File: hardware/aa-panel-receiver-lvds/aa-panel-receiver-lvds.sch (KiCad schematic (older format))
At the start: 100 parts, among them CN101 Conn_01x02, CN102 Conn_01x02, CN201 8P8C, CN202 Conn_01x08, CN251 Conn_01x08, CN301 8P8C, CN302 Conn_01x08, CN351 Conn_01x08, U101 CRE1S0505S3C, U201 ST26C32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

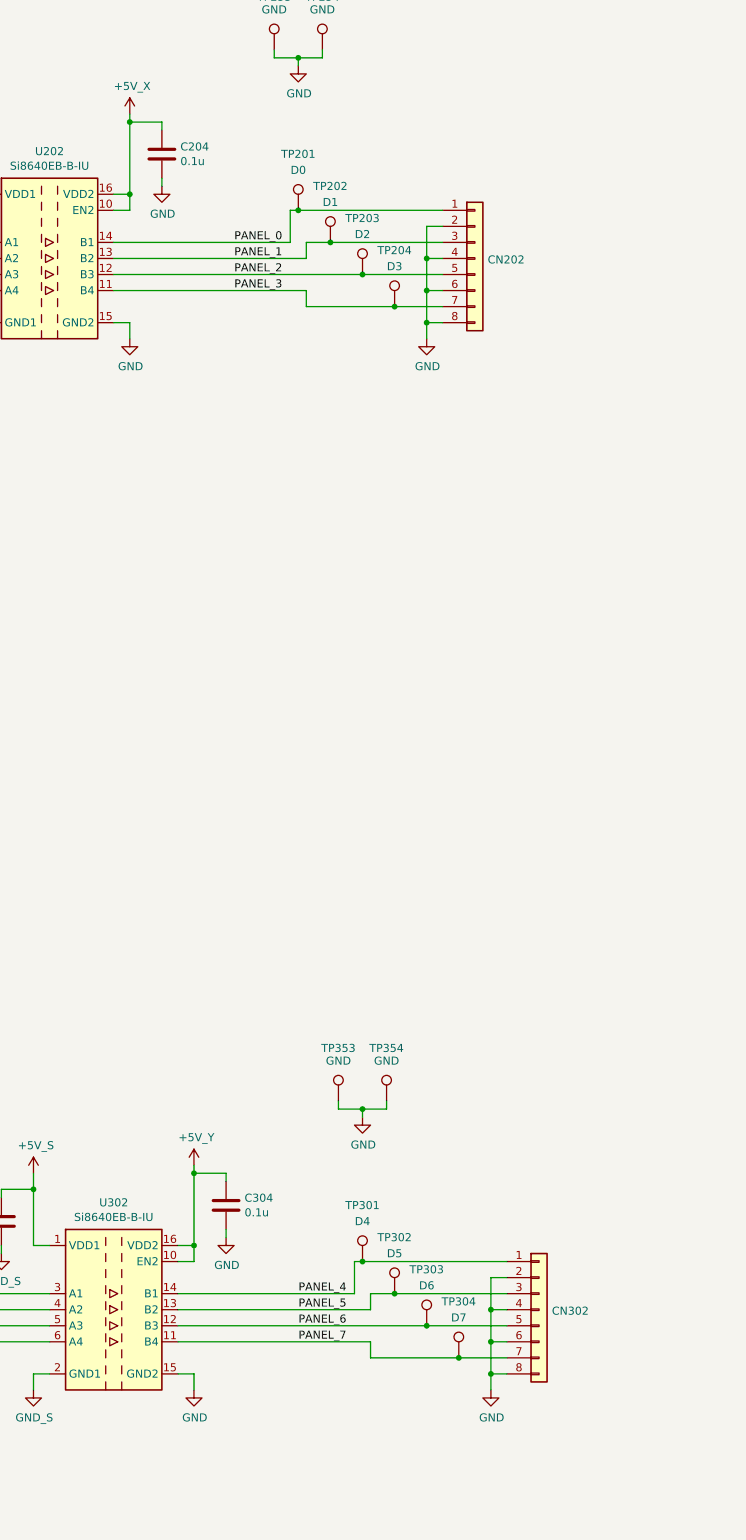
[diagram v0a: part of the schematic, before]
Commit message: Minor board updates to fix issues discovered during build
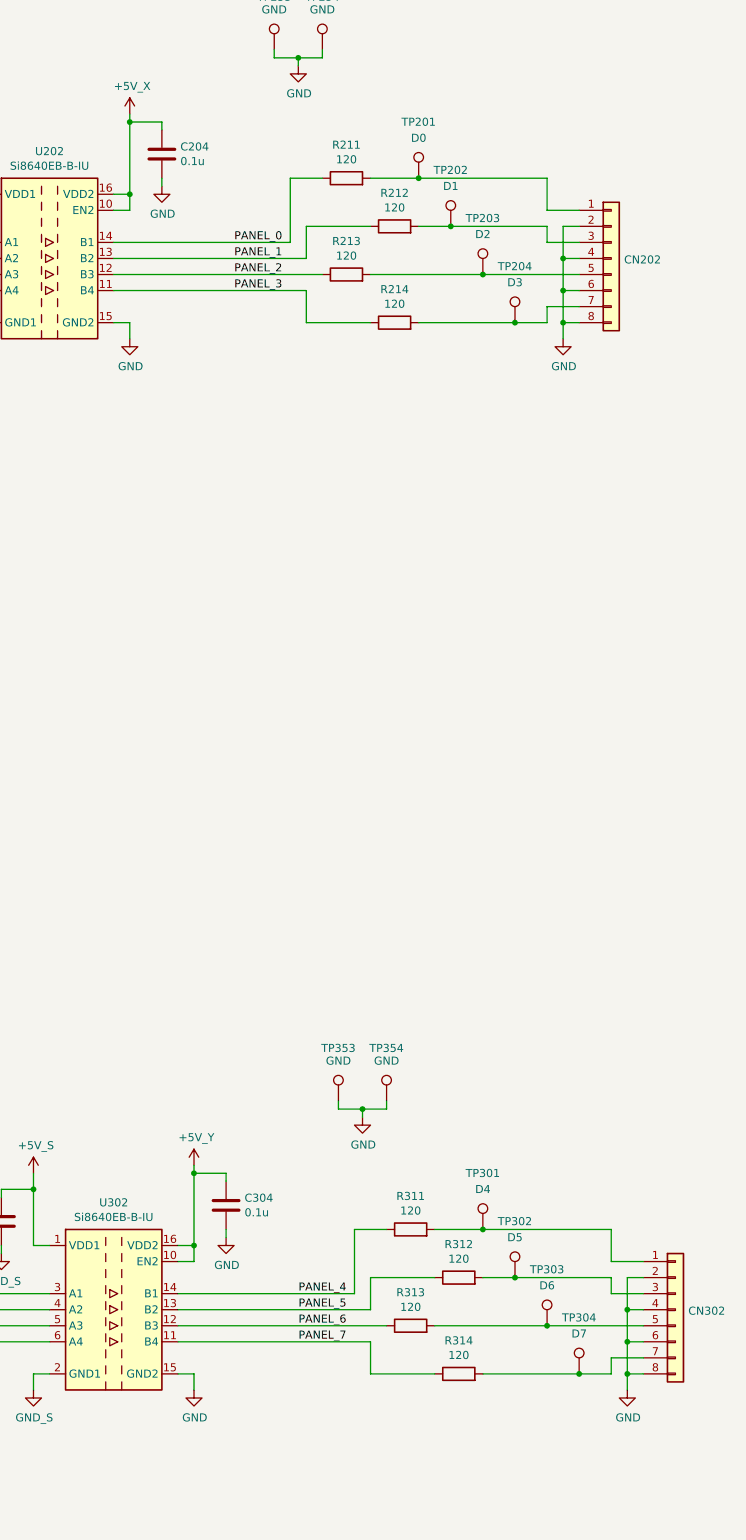
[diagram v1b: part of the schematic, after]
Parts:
- added R211, R212, R213, R214, R311, R312, R313, R314: 120, Resistor_SMD:R_0603_1608Metric, symbol Device:R
- C201, C301: footprint Capacitor_SMD:C_0603_1608Metric -> Capacitor_SMD:C_0805_2012Metric
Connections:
- net PANEL_0: now also R211.1; no longer CN202.1 (Pin_1), TP201.1
- net PANEL_1: now also R212.1; no longer CN202.3 (Pin_3), TP202.1
- net PANEL_2: now also R213.1; no longer CN202.5 (Pin_5), TP203.1
- net PANEL_3: now also R214.1; no longer CN202.7 (Pin_7), TP204.1
- net PANEL_4: now also R311.1; no longer CN302.1 (Pin_1), TP301.1
- net PANEL_5: now also R312.1; no longer CN302.3 (Pin_3), TP302.1
- net PANEL_6: now also R313.1; no longer CN302.5 (Pin_5), TP303.1
- net PANEL_7: now also R314.1; no longer CN302.7 (Pin_7), TP304.1
- new net: CN202.1 (Pin_1), R211.2, TP201.1
- new net: CN202.3 (Pin_3), R212.2, TP202.1
- new net: CN202.5 (Pin_5), R213.2, TP203.1
- new net: CN202.7 (Pin_7), R214.2, TP204.1
- new net: CN302.1 (Pin_1), R311.2, TP301.1
- new net: CN302.3 (Pin_3), R312.2, TP302.1
- new net: CN302.5 (Pin_5), R313.2, TP303.1
- new net: CN302.7 (Pin_7), R314.2, TP304.1
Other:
- moved on the sheet: CN202, CN302, TP201, TP202, TP203, TP204, TP301, TP302, TP303, TP304
